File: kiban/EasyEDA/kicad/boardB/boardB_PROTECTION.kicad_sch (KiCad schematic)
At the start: 34 parts, among them Q1 FS8205A, U2 BQ28Z620

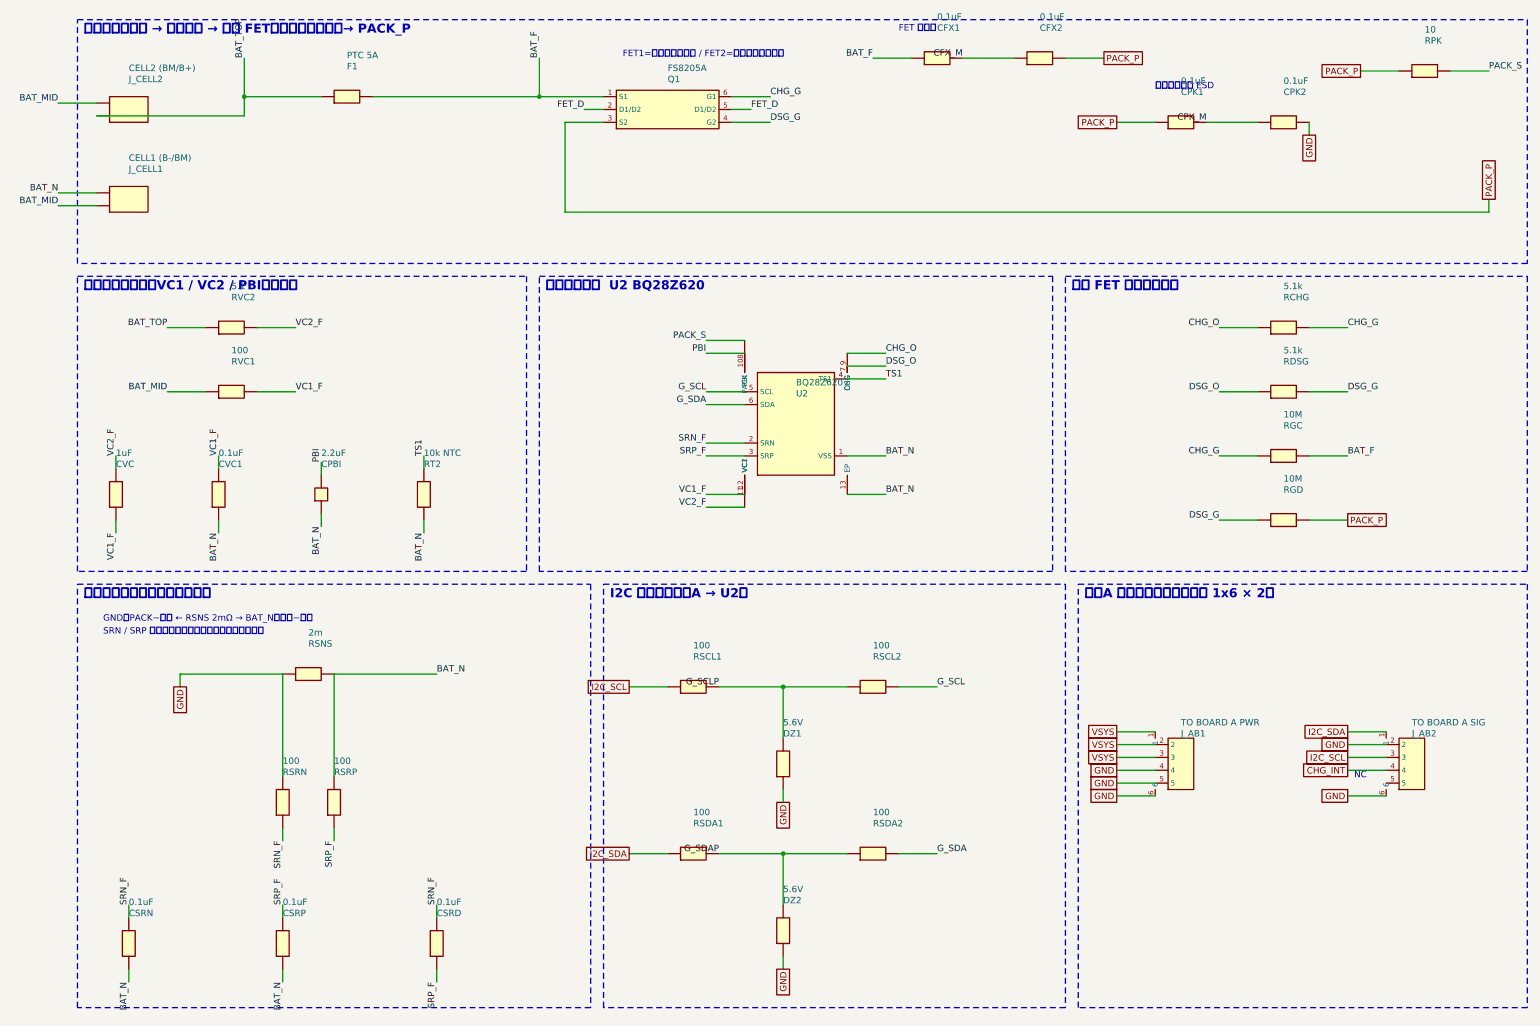
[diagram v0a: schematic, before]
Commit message: feat: KiCad 版の回路図に LCSC のシンボル・フットプリントを使う (easyeda2kicad)
- tools/kicad/lcsc_lib.py: LCSC 部品を easyeda2kicad で取得し、3D パスを直して KiCad 10 形式に更新、
  boardA / boardB に lcsc ライブラリを登録 (未取得の部品だけを、間隔を空けて取得)
- kicad_export.py: 取得したシンボルを、EasyEDA とピン位置が一致する向きで使い、フットプリントを割り当てる
  (合わない部品と未取得の部品は従来の矩形シンボル)。回転した部品の値の文字は横書きのまま
- 47 種類中 30 種類を取得 (残りは EasyEDA API の 403 で未取得)。111 部品中 82 部品が LCSC のシンボル
- kicad-cli のネットリストは基板A 23 / 基板B 43 ネットとも EasyEDA と一致
- 3D モデル (lcsc.3dshapes) と KiCad の .history/ は Git に入れない

Co-Authored-By: Claude Opus 5.5 <noreply@anthropic.com>
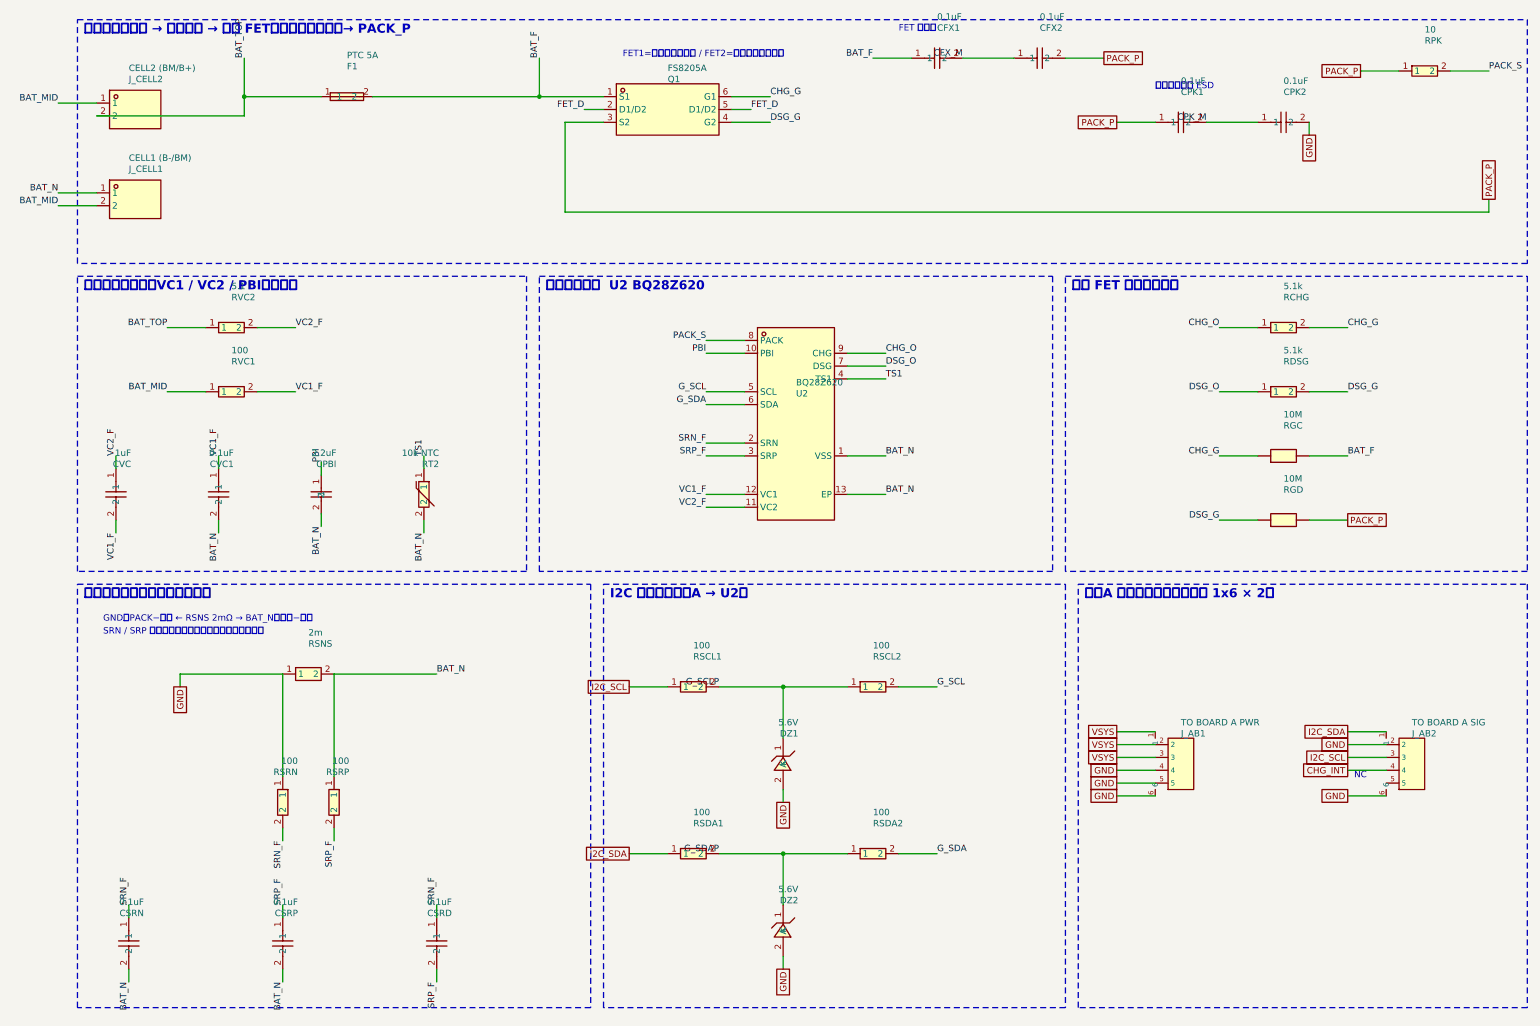
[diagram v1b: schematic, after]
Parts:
- CFX1, CFX2: footprint (none) -> lcsc:C0603; symbol gen:CFX_C1591_r0 -> lcsc:CL10B104KB8NNNC
- CPBI: footprint (none) -> lcsc:C0603; symbol gen:CPBI_C23630_r270 -> lcsc:CL10A225KO8NNNC
- CPK1, CPK2: footprint (none) -> lcsc:C0603; symbol gen:CPK_C1591_r0 -> lcsc:CL10B104KB8NNNC
- CSRD: footprint (none) -> lcsc:C0603; symbol gen:CSRD_C1591_r270 -> lcsc:CL10B104KB8NNNC
- CSRN: footprint (none) -> lcsc:C0603; symbol gen:CSRN_C1591_r270 -> lcsc:CL10B104KB8NNNC
- CSRP: footprint (none) -> lcsc:C0603; symbol gen:CSRP_C1591_r270 -> lcsc:CL10B104KB8NNNC
- CVC: footprint (none) -> lcsc:C0603; symbol gen:CVC_C15849_r270 -> lcsc:CL10A105KB8NNNC
- CVC1: footprint (none) -> lcsc:C0603; symbol gen:CVC_C1591_r270 -> lcsc:CL10B104KB8NNNC
- DZ1, DZ2: footprint (none) -> lcsc:SOD-323_L1.8-W1.3-LS2.5-RD; symbol gen:DZ_C22612_r270 -> lcsc:BZT52C5V6S
- F1: footprint (none) -> lcsc:FUSE-SMD_L8.0-W5.4; symbol gen:F_C108585_r0 -> lcsc:SMD2920P500TF_16
- J_CELL1, J_CELL2: footprint (none) -> lcsc:CONN-TH_B2B-XH-A-LF-SN; symbol gen:J_CELL_C158012_r0 -> lcsc:B2B-XH-A
- Q1: footprint (none) -> lcsc:SOT-23-6_L2.9-W1.6-P0.95-LS2.8-BR; symbol gen:Q_C908265_r0 -> lcsc:FS8205A_C908265
- RCHG: footprint (none) -> lcsc:R0603; symbol gen:RCHG_C23186_r0 -> lcsc:0603WAF5101T5E
- RDSG: footprint (none) -> lcsc:R0603; symbol gen:RDSG_C23186_r0 -> lcsc:0603WAF5101T5E
- RPK: footprint (none) -> lcsc:R0603; symbol gen:RPK_C22859_r0 -> lcsc:0603WAF100JT5E
- RSCL1, RSCL2: footprint (none) -> lcsc:R0603; symbol gen:RSCL_C22775_r0 -> lcsc:0603WAF1000T5E
- RSDA1, RSDA2: footprint (none) -> lcsc:R0603; symbol gen:RSDA_C22775_r0 -> lcsc:0603WAF1000T5E
- RSNS: footprint (none) -> lcsc:R1206; symbol gen:RSNS_C154630_r0 -> lcsc:LR1206-21R002F4
- RSRN: footprint (none) -> lcsc:R0603; symbol gen:RSRN_C22775_r270 -> lcsc:0603WAF1000T5E
- RSRP: footprint (none) -> lcsc:R0603; symbol gen:RSRP_C22775_r270 -> lcsc:0603WAF1000T5E
- RT2: footprint (none) -> lcsc:R0603; symbol gen:RT_C13564_r270 -> lcsc:NCP18XH103F03RB
- RVC1: footprint (none) -> lcsc:R0603; symbol gen:RVC_C22775_r0 -> lcsc:0603WAF1000T5E
- RVC2: footprint (none) -> lcsc:R0603; symbol gen:RVC_C25197_r0 -> lcsc:0603WAF510KT5E
- U2: footprint (none) -> lcsc:SON-12_L4.0-W2.5-P0.40-TL-EP; symbol gen:U_C20345237_r0 -> lcsc:BQ28Z620DRZR
